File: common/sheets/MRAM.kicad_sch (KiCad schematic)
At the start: 2 parts, among them U5 MR25H10

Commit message: add headers on sci board to accept camera hats
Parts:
- renumbered C28 to C69, U5 to U12
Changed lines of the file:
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@@
 		(on_board yes)
 		(dnp no)
-		(property "Reference" "C28"
+		(property "Reference" "C69"
 			(at 201.041 118.2116 0)
 			(effects
@@
 				)
 			)
-			(project "sci_board_wo_switches"
+			(project "sci_board_with_hat"
 				(path "/b4b2c88d-f6cd-4e60-862d-e21f68728580/f3d5c282-94c3-4259-817b-bad3ee4bc8e5"
-					(reference "C62")
+					(reference "C69")
 					(unit 1)
 				)
@@
 		(on_board yes)
 		(dnp no)
-		(property "Reference" "U5"
+		(property "Reference" "U12"
 			(at 158.75 104.6226 0)
 			(effects
@@
 				)
 			)
-			(project "sci_board_wo_switches"
+			(project "sci_board_with_hat"
 				(path "/b4b2c88d-f6cd-4e60-862d-e21f68728580/f3d5c282-94c3-4259-817b-bad3ee4bc8e5"
-					(reference "U11")
-					(unit 1)
-				)
+					(reference "U12")
+					(unit 1)
+				)

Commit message: switchless hat roughed in
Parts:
- renumbered C69 to C62, U12 to U11
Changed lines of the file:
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@@
 		(on_board yes)
 		(dnp no)
-		(property "Reference" "C69"
+		(property "Reference" "C62"
 			(at 201.041 118.2116 0)
 			(effects
@@
 				)
 			)
-			(project "sci_board_with_hat"
+			(project "sci_board_wo_switches"
 				(path "/b4b2c88d-f6cd-4e60-862d-e21f68728580/f3d5c282-94c3-4259-817b-bad3ee4bc8e5"
-					(reference "C69")
+					(reference "C62")
 					(unit 1)
 				)
@@
 		(on_board yes)
 		(dnp no)
-		(property "Reference" "U12"
+		(property "Reference" "U11"
 			(at 158.75 104.6226 0)
 			(effects
@@
 				)
 			)
-			(project "sci_board_with_hat"
+			(project "sci_board_wo_switches"
 				(path "/b4b2c88d-f6cd-4e60-862d-e21f68728580/f3d5c282-94c3-4259-817b-bad3ee4bc8e5"
-					(reference "U12")
-					(unit 1)
-				)
+					(reference "U11")
+					(unit 1)
+				)

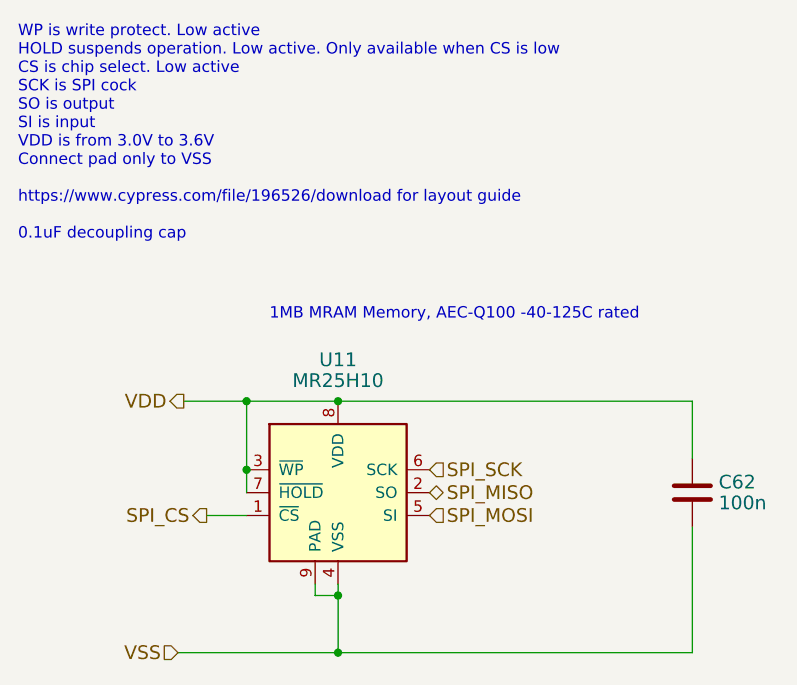
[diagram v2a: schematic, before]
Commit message: move camera connector to common
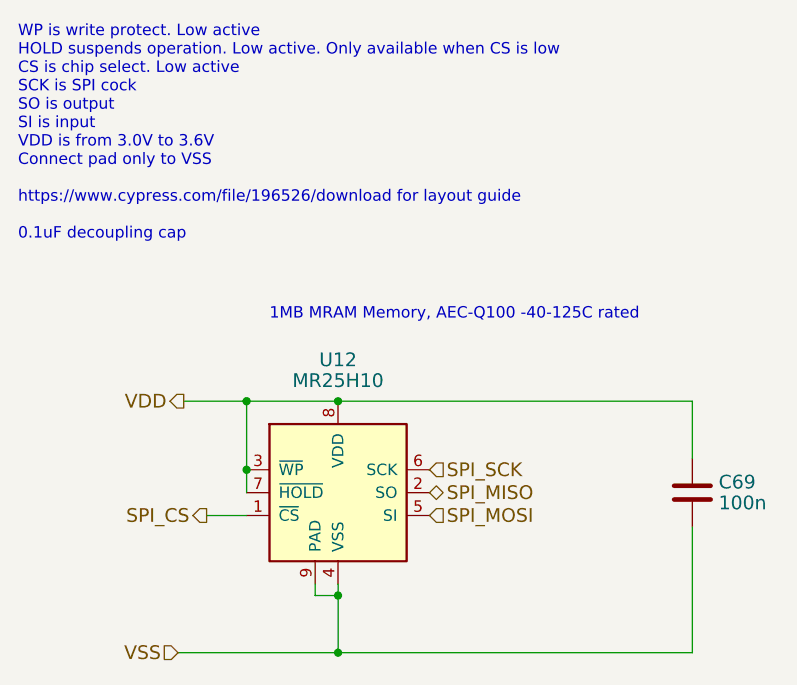
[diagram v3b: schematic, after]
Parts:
- renumbered C62 to C69, U11 to U12
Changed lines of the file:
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@@
 		(on_board yes)
 		(dnp no)
-		(property "Reference" "C62"
+		(property "Reference" "C69"
 			(at 201.041 118.2116 0)
 			(effects
@@
 				)
 			)
-			(project "sci_board_wo_switches"
+			(project "sci_board_with_hat"
 				(path "/b4b2c88d-f6cd-4e60-862d-e21f68728580/f3d5c282-94c3-4259-817b-bad3ee4bc8e5"
-					(reference "C62")
+					(reference "C69")
 					(unit 1)
 				)
@@
 		(on_board yes)
 		(dnp no)
-		(property "Reference" "U11"
+		(property "Reference" "U12"
 			(at 158.75 104.6226 0)
 			(effects
@@
 				)
 			)
-			(project "sci_board_wo_switches"
+			(project "sci_board_with_hat"
 				(path "/b4b2c88d-f6cd-4e60-862d-e21f68728580/f3d5c282-94c3-4259-817b-bad3ee4bc8e5"
-					(reference "U11")
-					(unit 1)
-				)
+					(reference "U12")
+					(unit 1)
+				)
